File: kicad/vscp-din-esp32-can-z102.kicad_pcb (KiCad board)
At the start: 2 copper layers, 47.8 x 84.8 mm, 33 parts, among them J1 Conn_01x05, J2 Conn_01x02, J3 Conn_01x06, J4 Conn_01x04, J5 Conn_01x04, J6 Conn_01x03, U1 ESP32-C3-WROOM-02-N4, U2 LM2575-3.3BT, U3 SN65HVD232, U4 R-78B3.3-1.0 (Recom)

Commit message: Added images for rev B
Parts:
- moved J1 0.30 mm to (142.1, 81.2)
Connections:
- U1 pad 10: /rxcan -> unconnected-(U1-Pad10)
- U1 pad 15: /io3 -> /rxcan
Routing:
- net /rxcan: track 18.8 -> 24.4 mm
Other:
- board text added: "Rev B"
- board text removed: "Rev A"
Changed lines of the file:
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@@
   (net 21 "/tx")
   (net 22 "Net-(J3-Pad4)")
-  (net 23 "Net-(J4-Pad1)")
-  (net 24 "Net-(L1-Pad1)")
+  (net 23 "Net-(D1-Pad2)")
+  (net 24 "Net-(D2-Pad1)")
   (net 25 "Net-(D3-Pad1)")
   (net 26 "Net-(D3-Pad2)")
-  (net 27 "Net-(R11-Pad2)")
+  (net 27 "Net-(J6-Pad2)")
   (net 28 "Net-(J3-Pad1)")
-  (net 29 "/io3")
+  (net 29 "unconnected-(U1-Pad10)")
   (net 30 "/io4")
   (net 31 "/io5")
@@
       (net 1 "+3V3") (pintype "passive"))
     (pad "2" smd roundrect (at 0.9125 0 180) (size 1.025 1.4) (layers "F.Cu" "F.Paste" "F.Mask") (roundrect_rratio 0.243902439)
-      (net 27 "Net-(R11-Pad2)") (pintype "passive"))
+      (net 27 "Net-(J6-Pad2)") (pintype "passive"))
     (model "${KICAD6_3DMODEL_DIR}/Resistor_SMD.3dshapes/R_0805_2012Metric.wrl"
       (offset (xyz 0 0 0))
@@
       (net 7 "/leda") (pinfunction "Pin_1") (pintype "passive"))
     (pad "2" thru_hole oval (at 0 2.54 180) (size 1.7 1.7) (drill 1) (layers *.Cu *.Mask)
-      (net 27 "Net-(R11-Pad2)") (pinfunction "Pin_2") (pintype "passive"))
+      (net 27 "Net-(J6-Pad2)") (pinfunction "Pin_2") (pintype "passive"))
     (pad "3" thru_hole oval (at 0 5.08 180) (size 1.7 1.7) (drill 1) (layers *.Cu *.Mask)
       (net 6 "/ledb") (pinfunction "Pin_3") (pintype "passive"))
@@
       (net 18 "+28V") (pinfunction "VIN") (pintype "power_in"))
     (pad "2" smd rect (at -5.775 -1.7) (size 4.6 1.1) (layers "F.Cu" "F.Paste" "F.Mask")
-      (net 24 "Net-(L1-Pad1)") (pinfunction "OUT") (pintype "output"))
+      (net 24 "Net-(D2-Pad1)") (pinfunction "OUT") (pintype "output"))
     (pad "3" smd rect (at 3.375 0) (size 9.4 10.8) (layers "F.Cu" "F.Mask")
       (net 2 "GND") (pinfunction "GND") (pintype "power_in"))
@@
       (net 2 "GND") (pinfunction "GND") (pintype "power_in"))
     (pad "10" smd rect (at 8.75 6 90) (size 1.5 0.9) (layers "F.Cu" "F.Paste" "F.Mask")
-      (net 12 "/rxcan") (pinfunction "IO10") (pintype "bidirectional"))
+      (net 29 "unconnected-(U1-Pad10)") (pinfunction "IO10") (pintype "bidirectional"))
     (pad "11" smd rect (at 8.75 4.5 90) (size 1.5 0.9) (layers "F.Cu" "F.Paste" "F.Mask")
       (net 20 "/rx") (pinfunction "RXD") (pintype "bidirectional"))
@@
       (net 10 "Net-(R2-Pad1)") (pinfunction "IO19") (pintype "bidirectional"))
     (pad "15" smd rect (at 8.75 -1.5 90) (size 1.5 0.9) (layers "F.Cu" "F.Paste" "F.Mask")
-      (net 29 "/io3") (pinfunction "IO3") (pintype "bidirectional"))
+      (net 12 "/rxcan") (pinfunction "IO3") (pintype "bidirectional"))
     (pad "16" smd rect (at 8.75 -3 90) (size 1.5 0.9) (layers "F.Cu" "F.Paste" "F.Mask")
       (net 15 "/MISO") (pinfunction "IO2") (pintype "bidirectional"))
@@
     (fp_line (start 0.50118 0.00102) (end 1.4994 0.00102) (layer "F.Fab") (width 0.1))
     (pad "1" smd rect (at -2.5 0 90) (size 3.5 1.8) (layers "F.Cu" "F.Paste" "F.Mask")
-      (net 24 "Net-(L1-Pad1)") (pinfunction "K") (pintype "passive"))
+      (net 24 "Net-(D2-Pad1)") (pinfunction "K") (pintype "passive"))
     (pad "2" smd rect (at 2.5 0 90) (size 3.5 1.8) (layers "F.Cu" "F.Paste" "F.Mask")
       (net 2 "GND") (pinfunction "A") (pintype "passive"))
@@
     (fp_circle (center 0 0) (end 0 -5.6) (layer "F.Fab") (width 0.1) (fill none))
     (pad "1" smd rect (at -4.85 0) (size 2.9 5.4) (layers "F.Cu" "F.Paste" "F.Mask")
-      (net 24 "Net-(L1-Pad1)") (pinfunction "1") (pintype "passive"))
+      (net 24 "Net-(D2-Pad1)") (pinfunction "1") (pintype "passive"))
     (pad "2" smd rect (at 4.85 0) (size 2.9 5.4) (layers "F.Cu" "F.Paste" "F.Mask")
       (net 1 "+3V3") (pinfunction "2") (pintype "passive"))
@@
     (fp_line (start 0 0) (end -0.8 -1.2) (layer "F.Fab") (width 0.1))
     (pad "1" thru_hole roundrect (at 0 0 180) (size 1.8 3.6) (drill 1.2) (layers *.Cu *.Mask) (roundrect_rratio 0.1388888889)
-      (net 23 "Net-(J4-Pad1)") (pinfunction "Pin_1") (pintype "passive"))
+      (net 23 "Net-(D1-Pad2)") (pinfunction "Pin_1") (pintype "passive"))
     (pad "2" thru_hole oval (at 3.81 0 180) (size 1.8 3.6) (drill 1.2) (layers *.Cu *.Mask)
       (net 26 "Net-(D3-Pad2)") (pinfunction "Pin_2") (pintype "passive"))
@@
   )
   (footprint "Connector_PinHeader_2.54mm:PinHeader_1x05_P2.54mm_Vertical" (layer "F.Cu")
-    (at 142.375 81.25 90)
+    (at 142.075 81.25 90)
     (descr "Through hole straight pin header, 1x05, 2.54mm pitch, single row")
     (tags "Through hole pin header THT 1x05 2.54mm single row")
@@
       (net 18 "+28V") (pinfunction "K") (pintype "passive"))
     (pad "2" smd rect (at 1.65 0 180) (size 0.9 1.2) (layers "F.Cu" "F.Paste" "F.Mask")
-      (net 23 "Net-(J4-Pad1)") (pinfunction "A") (pintype "passive"))
+      (net 23 "Net-(D1-Pad2)") (pinfunction "A") (pintype "passive"))
     (model "${KICAD6_3DMODEL_DIR}/Diode_SMD.3dshapes/D_SOD-123.wrl"
       (offset (xyz 0 0 0))
@@
     (effects (font (size 1.5 1.5) (thickness 0.3)))
   )
-  (gr_text "Rev A" (at 125.65 131.8) (layer "F.SilkS")
+  (gr_text "Rev B" (at 125.65 131.8) (layer "F.SilkS")
     (effects (font (size 1.5 1.5) (thickness 0.3)))
   )
@@
   (segment (start 140.55 108) (end 138.25 110.3) (width 0.25) (layer "F.Cu") (net 11))
   (segment (start 140.55 85.664282) (end 140.55 108) (width 0.25) (layer "F.Cu") (net 11))
-  (segment (start 129.725 82.905) (end 131.57 84.75) (width 0.25) (layer "F.Cu") (net 12))
-  (segment (start 139.75 85.5) (end 139.75 93.25) (width 0.25) (layer "F.Cu") (net 12))
-  (segment (start 131.57 84.75) (end 139 84.75) (width 0.25) (layer "F.Cu") (net 12))
-  (segment (start 139 84.75) (end 139.75 85.5) (width 0.25) (layer "F.Cu") (net 12))
+  (segment (start 129.725 82.905) (end 131.569989 84.749989) (width 0.25) (layer "F.Cu") (net 12))
+  (segment (start 131.569989 84.749989) (end 138.999989 84.749989) (width 0.25) (layer "F.Cu") (net 12))
+  (segment (start 138.475386 86.2) (end 137.525386 87.15) (width 0.25) (layer "F.Cu") (net 12))
+  (segment (start 137.525386 87.15) (end 134.05 87.15) (width 0.25) (layer "F.Cu") (net 12))
+  (segment (start 132.25 91.1) (end 132.25 93.25) (width 0.25) (layer "F.Cu") (net 12))
+  (segment (start 139.5 86.2) (end 138.475386 86.2) (width 0.25) (layer "F.Cu") (net 12))
+  (segment (start 132.9 90.45) (end 132.25 91.1) (width 0.25) (layer "F.Cu") (net 12))
+  (segment (start 134.05 87.15) (end 132.9 88.3) (width 0.25) (layer "F.Cu") (net 12))
+  (segment (start 138.999989 84.749989) (end 139.5 85.25) (width 0.25) (layer "F.Cu") (net 12))
+  (segment (start 139.5 85.25) (end 139.5 86.2) (width 0.25) (layer "F.Cu") (net 12))
+  (segment (start 132.9 88.3) (end 132.9 90.45) (width 0.25) (layer "F.Cu") (net 12))
   (segment (start 135.7 104.65) (end 139.3 104.65) (width 0.25) (layer "F.Cu") (net 13))
   (segment (start 133.75 106.6) (end 135.7 104.65) (width 0.25) (layer "F.Cu") (net 13))

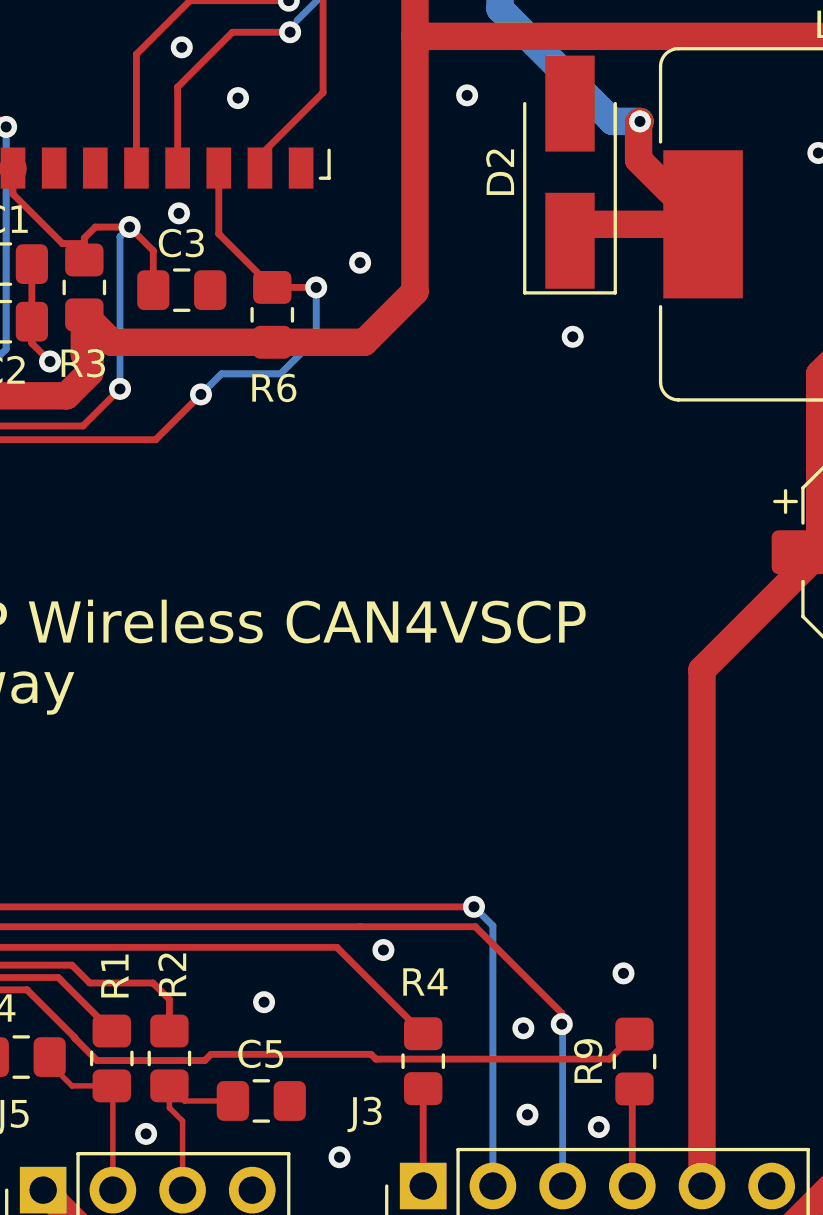
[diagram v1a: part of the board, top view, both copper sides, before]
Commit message: txcan routed to Flash pin instead of io8
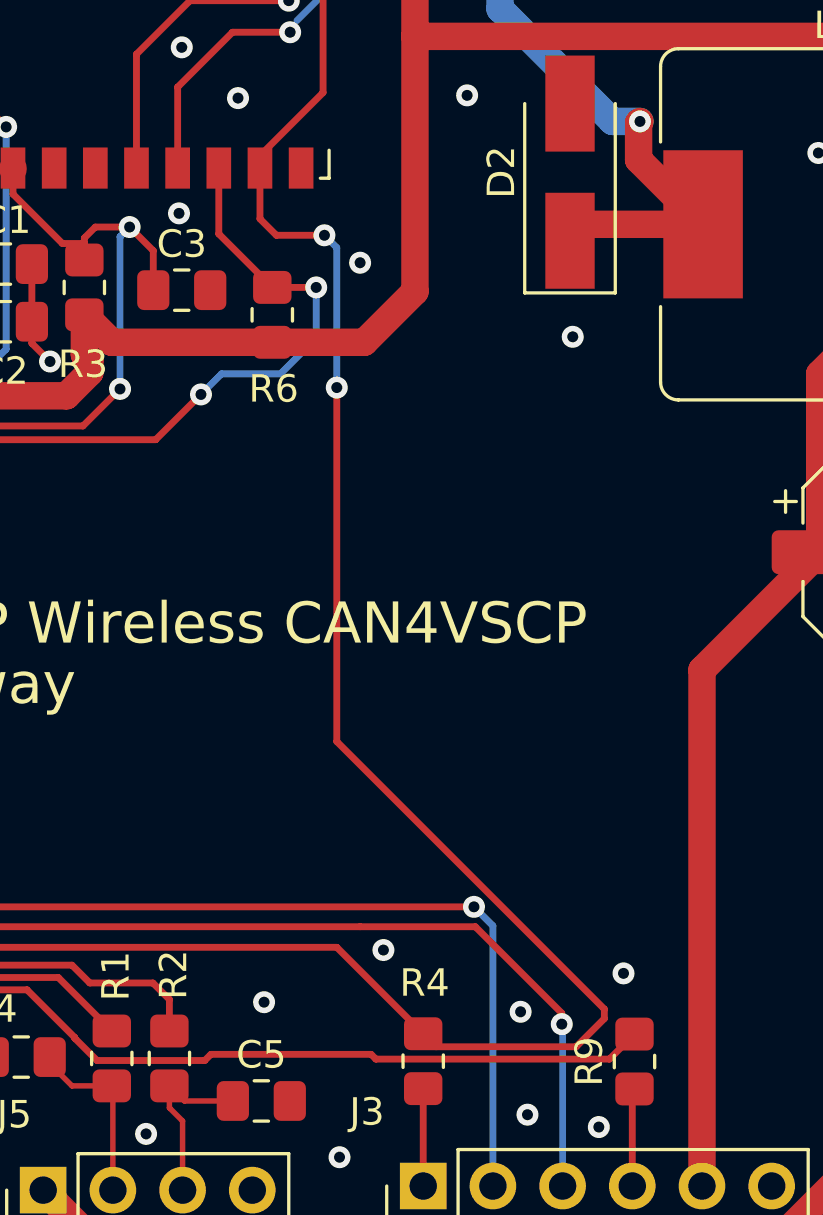
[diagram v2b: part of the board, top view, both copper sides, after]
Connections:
- R4 pad 2: /flash -> /txcan
- R6 pad 2: /flash -> /io8
- U1 pad 7: /flash -> /io8
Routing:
- net /txcan: track 41.1 -> 148.1 mm, vias 0 -> 4
- net /flash: track 68.1 -> 0.00 mm, vias 2 -> 0
- net /io8: track 0.00 -> 4.71 mm

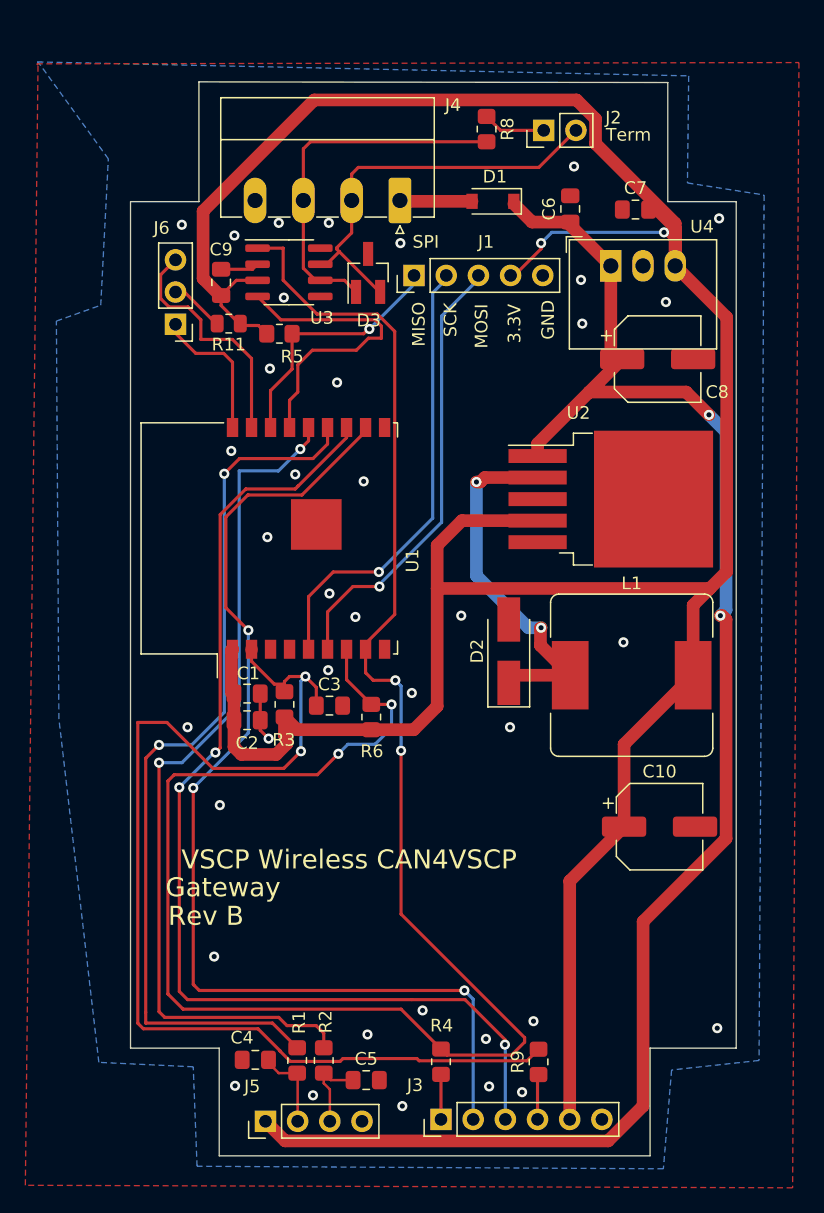
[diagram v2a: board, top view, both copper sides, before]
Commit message: J4 moved closer to edge.
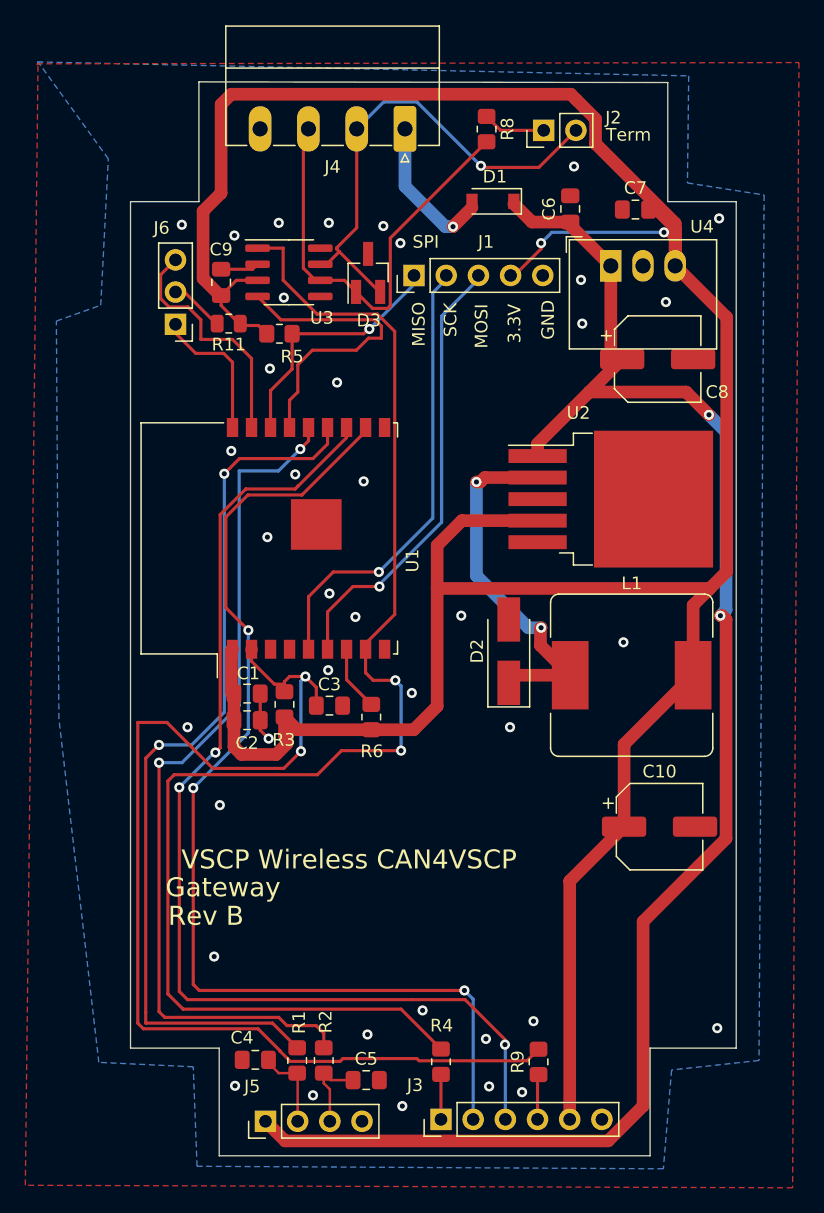
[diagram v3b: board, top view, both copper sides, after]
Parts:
- moved J4 5.66 mm to (141.4, 69.7)
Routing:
- net /txcan: track 148.1 -> 110.8 mm, vias 4 -> 2
- net Net-(D1-Pad2): track 5.72 -> 12.3 mm, vias 0 -> 1
- net Net-(D3-Pad1): track 29.0 -> 35.5 mm
- net Net-(D3-Pad2): track 32.3 -> 38.5 mm, vias 0 -> 1
- net +3V3: track 232.7 -> 237.1 mm
- net GND: vias 38 -> 39

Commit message: Added connector and resistor for BUS_OFF LED connector.
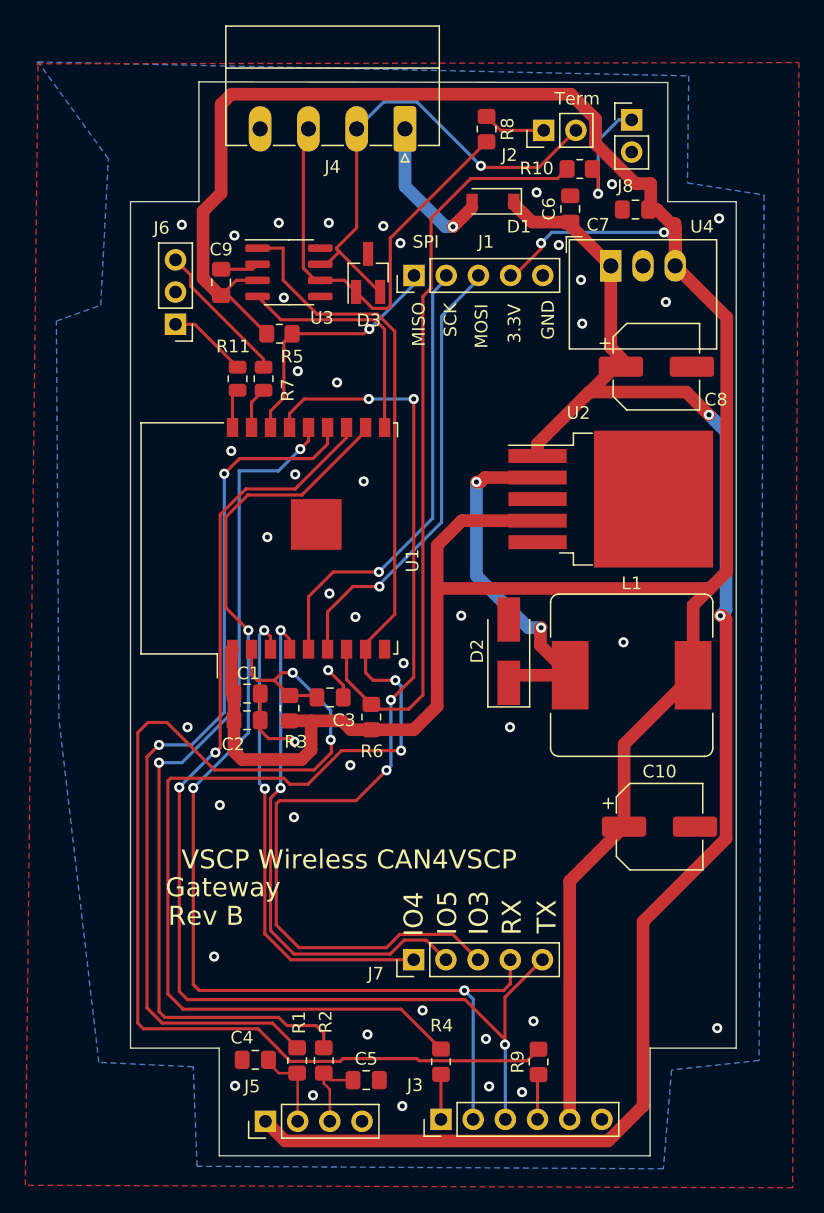
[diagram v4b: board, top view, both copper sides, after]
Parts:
- added J7: Conn_01x05, Connector_PinHeader_2.54mm:PinHeader_1x05_P2.54mm_Vertical, F.Cu at (142.1, 135.2)
- added J8: Conn_01x02, Connector_PinHeader_2.54mm:PinHeader_1x02_P2.54mm_Vertical, F.Cu at (159.2, 69.0)
- added R10: 330R, Resistor_SMD:R_0805_2012Metric_Pad1.20x1.40mm_HandSolder, F.Cu at (155.2, 72.8)
- added R7: 470, Resistor_SMD:R_0805_2012Metric, F.Cu at (130.2, 89.4)
- moved R11 4.41 mm to (128.2, 89.4), turned to 90 degrees
- moved C3 0.65 mm to (135.4, 114.5)
- moved C8 0.61 mm to (161.2, 88.5)
- moved R3 0.50 mm to (132.2, 115.4)
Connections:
- net /io8 renamed /boff
- J6 pad 1: /leda -> Net-(J6-Pad1)
- J6 pad 2: Net-(J6-Pad2) -> GND
- J6 pad 3: /ledb -> Net-(J6-Pad3)
- R11 pad 1: +3V3 -> /leda
- R11 pad 2: Net-(J6-Pad2) -> Net-(J6-Pad1)
- U1 pad 10: unconnected-(U1-Pad10) -> /rxcan
- U1 pad 15: /rxcan -> /io3
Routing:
- net /io3: track 0.00 -> 78.9 mm, vias 0 -> 4
- net /boff: track 5.16 -> 60.1 mm
- net /io5: track 0.00 -> 41.5 mm, vias 0 -> 2
- net /io4: track 0.00 -> 38.6 mm, vias 0 -> 2
- net /ledb: track 19.0 -> 3.33 mm
- net Net-(J6-Pad3): track 0.00 -> 11.3 mm
- net Net-(J8-Pad1): track 0.00 -> 9.66 mm, vias 0 -> 1
- net /leda: track 11.3 -> 3.10 mm
- net /tx: track 85.9 -> 93.8 mm
- net Net-(J6-Pad1): track 0.00 -> 6.30 mm
- net /rx: track 85.6 -> 91.3 mm
- net /rxcan: track 24.4 -> 18.8 mm
- net GND: track 6.86 -> 11.7 mm, vias 39 -> 43
- net Net-(J6-Pad2): track 4.44 -> 0.00 mm
- net /reset: track 87.7 -> 91.3 mm
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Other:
- board text added: "IO3"
- board text added: "IO4"
- board text added: "IO5"

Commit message: Rev B away for production
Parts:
- added D4: 1N5819, Diode_SMD:D_SOD-123, F.Cu at (159.8, 137.0)
- added J9: Conn_01x02, Connector_PinHeader_2.54mm:PinHeader_1x02_P2.54mm_Vertical, F.Cu at (135.1, 124.6)
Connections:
- J5 pad 1: +28V -> Net-(D4-A)
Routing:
- net +28V: track 128.2 -> 85.3 mm
- net Net-(D4-A): track 0.00 -> 39.7 mm
- net GND: track 11.7 -> 25.7 mm, vias 43 -> 51
- net /reset: track 91.3 -> 98.9 mm
- net Net-(J2-Pin_2): track 38.5 -> 39.2 mm
- net /txcan: track 111.2 -> 111.8 mm
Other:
- board text added: "CAN4VSCP Frankfurt Wifi"
- board text added: "vscp.org"
- board text added: "www.grodansparadis.com"
- board text removed: "Gateway"
- board text removed: "VSCP Wireless CAN4VSCP"
- board text removed: "http://www.grodansparadis.com"
